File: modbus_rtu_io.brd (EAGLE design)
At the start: 108 x 67.9 mm, 60 parts, among them IC1 MAX3485ESA, IC5 ATMEGA48/88/168-PU, K1 AQY27SMD, K2 AQY22SOP, K3 G6D-1A-ASI12VDC, K4 RP418005, K5 AQG12105, K7 G6D-1A-ASI12VDC, K8 AQY22SOP, T1 BC846, T2 BC846, T4 BC846

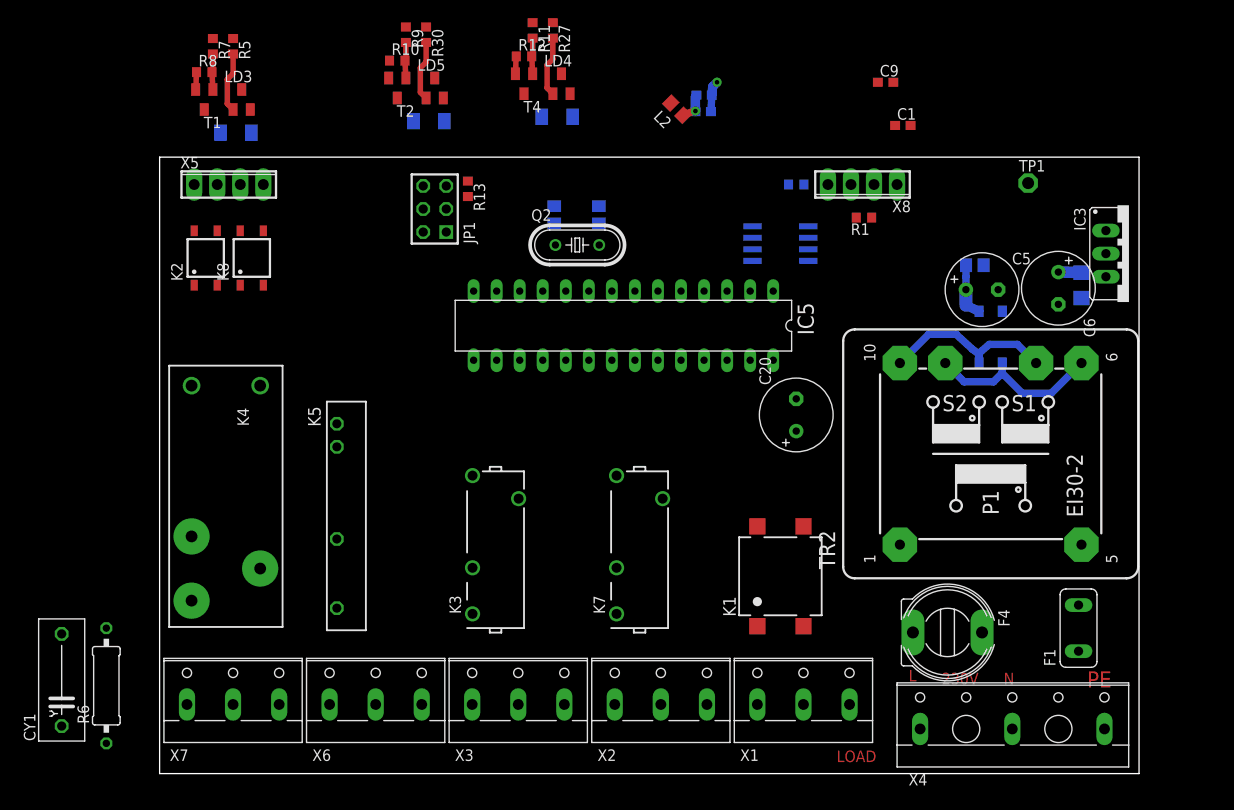
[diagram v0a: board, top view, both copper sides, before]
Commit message: Relais geändert, Routing angefangen
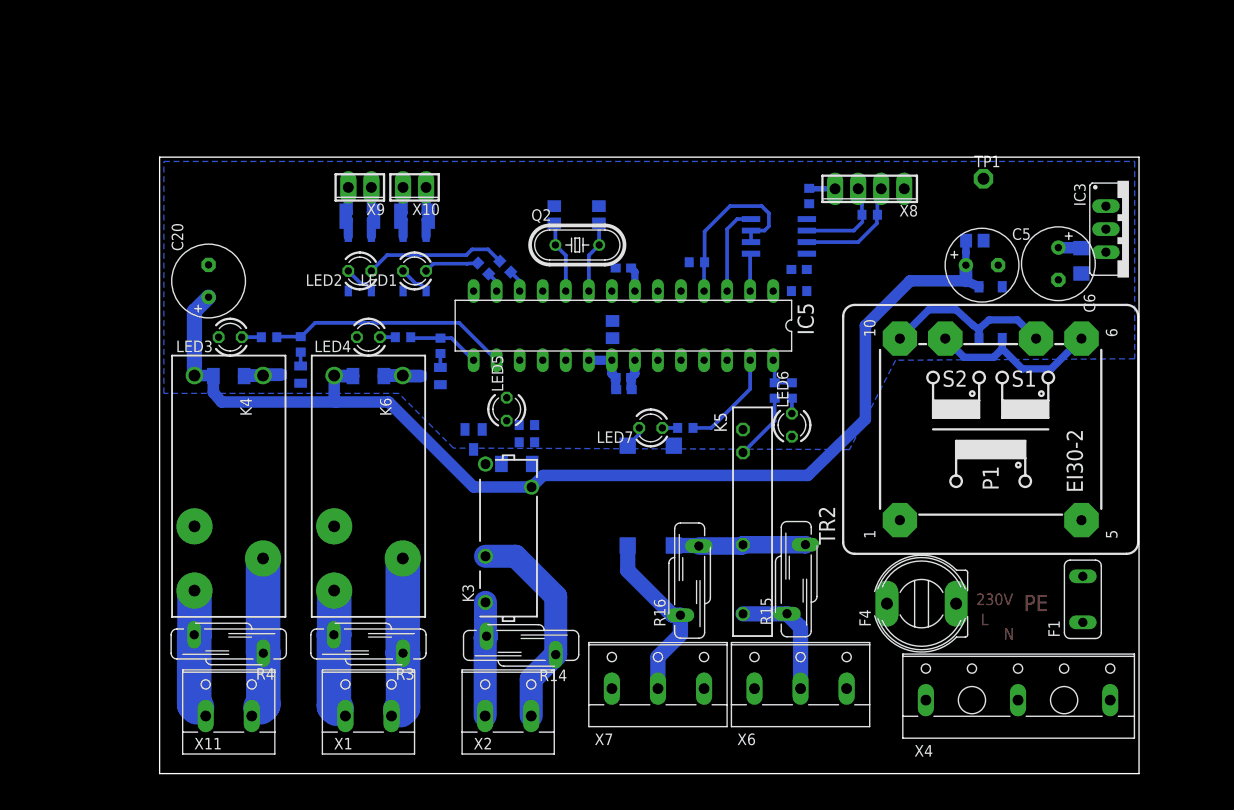
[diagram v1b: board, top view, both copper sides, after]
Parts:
- removed CY1: (no value), rcl:YC10B5
- removed JP1: AVR-ISP-6, atmel:AVR-ISP-6
- removed K7: G6D-1A-ASI12VDC, relay:G6D
- removed LD3, LD4, LD5: PL006-WCR12, led:SOT23
- removed R12: 100K, rcl:R0603
- removed X3: (no value), con-wago-508:W237-133
- removed X5: (no value), con-phoenix-254:4POL254
- added K6: RP418005, relay:RT-C/O12A3.5
- added LED1, LED2, LED3, LED4, LED5, LED6, LED7: (no value), led:LED3MM
- added R14, R15, R16, R3, R4: S10K40, varistor:S10K40
- added R17, R18: VARISTORCN1210, varistor:CT/CN1210
- added R19, R20, R21: 120, rcl:R0603
- added X10, X9: (no value), con-phoenix-254:2POL254
- added X11: (no value), con-wago-508:W237-132
- R10: value 100K -> 120
- R6: value (none) -> 120; device rcl:0309/12 -> rcl:R0603
- R8: value 100K -> 47K
- X1, X2: device con-wago-508:W237-133 -> con-wago-508:W237-132
- moved R6 80.5 mm to (67.8, 42.2), flipped to the bottom, turned to 270 degrees
- moved C20 66.4 mm to (5.40, 54.3)
- moved R8 58.2 mm to (59.2, 56.4), flipped to the bottom
- moved R10 56.7 mm to (69.7, 42.2), flipped to the bottom, turned to 270 degrees
- moved X1 48.0 mm to (23.0, 6.99)
- moved X7 46.9 mm to (54.9, 10.0)
- moved X6 46.9 mm to (70.6, 10.0)
- moved R9 46.9 mm to (40.5, 36.5), flipped to the bottom, turned to 0 degrees
- moved K5 44.8 mm to (64.3, 27.8)
- moved R30 44.4 mm to (40.5, 38.4), flipped to the bottom, turned to 0 degrees
- moved T2 39.6 mm to (34.6, 36.8), flipped to the bottom
- moved D3 39.0 mm to (39.4, 34.1)
- moved R13 38.2 mm to (70.5, 53.2), flipped to the bottom, turned to 180 degrees
- moved R27 37.6 mm to (26.8, 48.1), flipped to the bottom, turned to 0 degrees
- moved R11 36.2 mm to (31.0, 47.1), flipped to the bottom
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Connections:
- removed net DATA: IC5.18, JP1.1
- removed net MOSI: IC5.17, JP1.4
- removed net SCK: IC5.19, JP1.3
- new net AQG12105: IC5.28, R10.1, R6.1
- new net AQY27SMD: IC5.27, R19.1
- new net N$24: K6.11, R3.1, X1.2
- new net N$25: K3.7, R14.2, X2.1
- new net N$26: K3.5, R14.1, X2.2
- new net N$27: K5.O2, R15.1, X6.2
- new net N$29: K1.4, R16.1, X7.2
- new net N$30: K5.+, R6.2
- new net N$31: K1.1, LED7.K
- new net N$32: K2.1, LED2.K
- new net N$35: K8.1, LED1.K
- new net N$37: IC5.12, R20.2
- new net N$38: IC5.13, R21.2
- new net N$4: K4.11, R4.1, X11.2
- new net N$41: LED1.A, R21.1
- new net N$42: LED2.A, R20.1
- new net N$43: LED7.A, R19.2
- new net N$44: LED6.K, R10.2
- new net N$5: K4.14, R4.2, X11.1
- new net N$6: K6.14, R3.2, X1.1
- net +12V: now also K6.A1; no longer K7.13
- net +5V: no longer JP1.2
- net GND: now also K1.2, K2.2, K5.-, K8.2, LED3.K, LED4.K, LED5.K, LED6.A, R8.2; no longer CY1.2, JP1.6, LD3.3, LD4.3, LD5.3, R10.1, R12.1, R6.2, R8.1
- net N$13: no longer R12.2
- net N$14: now also K6.A2; no longer K7.1
- net N$15: now also IC5.4, R8.1
- net N$16: now also R18.1, X10.1; no longer X5.3
- net N$18: now also R18.2, X10.2; no longer X5.4
- net N$2: no longer R10.2
- net N$20: now also R17.1, X9.1; no longer X5.1
- net N$21: now also R17.2, X9.2; no longer X5.2
- net N$28: now also X6.3, X7.3
- net N$3: now also LED3.A; no longer LD3.1
- net N$33: now also K1.3, K5.O1, R15.2, R16.2
- net N$34: now also LED4.A; no longer LD4.1
- net N$36: now also IC5.16
- net N$39: now also IC5.15
- net N$40: now also IC5.17
- net N$50: now also LED5.A; no longer LD5.1
- net N$55: no longer JP1.5
- net N$7: no longer R8.2
- net PE: now also X6.1, X7.1; no longer CY1.1, R6.1
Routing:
- net +12V: track 6.02 -> 127.2 mm
- net N$36: track 0.00 -> 26.6 mm
- net N$26: track 0.00 -> 23.9 mm
- net N$15: track 0.00 -> 20.0 mm
- net N$29: track 0.00 -> 19.7 mm
- net N$24: track 0.00 -> 16.9 mm
- net N$4: track 0.00 -> 16.6 mm
- net N$42: track 0.00 -> 15.7 mm
- net N$33: track 0.00 -> 14.6 mm
- net N$27: track 0.00 -> 13.7 mm
- net N$6: track 0.00 -> 13.2 mm
- net N$5: track 0.00 -> 13.0 mm
- net N$25: track 0.00 -> 12.6 mm
- net RS485_B: track 0.00 -> 12.6 mm
- net AQY27SMD: track 0.00 -> 11.2 mm
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- added copper zone on layer 16, net GND
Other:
- board text removed: "LOAD"

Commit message: routing fertig
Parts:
- removed X4: (no value), con-wago-508:W237-3N
- added C3, C7, C8: 100nF, rcl:C0603
- added LED8: (no value), led:LED3MM
- added R12, R23, R24: 120, rcl:R0603
- added R22: 10K, rcl:R0603
- added SL1: (no value), con-amp-quick:03P
- added SL2: (no value), con-amp-quick:02P
- added X3: GMSTBV3, con-phoenix-762:GMSTBV3
- moved TP1 14.4 mm to (105.3, 65.2)
- moved IC3 14.4 mm to (93.2, 64.5), turned to 0 degrees
- moved F1 12.9 mm to (88.9, 19.4)
- moved X9 9.00 mm to (13.2, 63.2)
- moved R17 8.90 mm to (13.2, 61.1)
- moved K2 8.89 mm to (13.2, 56.2)
- moved LED2 8.89 mm to (13.2, 55.4)
- moved X10 8.07 mm to (20.2, 63.2)
- moved R18 7.94 mm to (20.2, 61.1)
- moved K8 7.94 mm to (20.2, 56.2)
- moved LED1 7.94 mm to (20.2, 55.4)
- moved R9 7.31 mm to (34.4, 40.6)
- moved F4 4.00 mm to (80.0, 18.3)
- moved R30 3.62 mm to (37.6, 40.6), turned to 180 degrees
- moved R1 2.93 mm to (76.0, 59.7)
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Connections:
- new net N$45: R12.1, X8.1
- new net N$51: LED8.K, R22.2
- new net N$53: C7.1, IC5.6, R23.1, SL1.1
- new net N$56: C8.2, IC5.23, R24.2, SL2.2
- net +12V: now also R12.2
- net +5V: now also C3.1, LED8.A, R23.2, SL1.3, SL2.1
- net GND: now also C3.2, C7.2, C8.1, R22.1, R24.1, SL1.2
- net L: now also X3.2; no longer X4.1
- net N$23: now also TR2.1; no longer TR2.5
- net N$28: now also TR2.5, X3.3; no longer TR2.1, X4.2
- net PE: now also X3.1; no longer X4.3
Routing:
- net N$28: track 0.00 -> 76.6 mm
- net PE: track 0.00 -> 51.0 mm
- net N$56: track 0.00 -> 37.9 mm
- net +5V: track 5.26 -> 41.3 mm, vias 0 -> 1
- net N$26: track 23.9 -> 45.7 mm
- net L: track 0.00 -> 18.1 mm
- net N$49: track 0.00 -> 15.7 mm
- net N$47: track 0.00 -> 15.6 mm
- net +12V: track 127.2 -> 142.4 mm
- net N$48: track 0.00 -> 12.3 mm
- net N$46: track 0.00 -> 11.9 mm
- net N$23: track 0.00 -> 11.0 mm
- net N$25: track 12.6 -> 23.0 mm
- net N$53: track 0.00 -> 8.97 mm
- net N$42: track 15.7 -> 24.6 mm
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- added copper zone on layer 1, net +5V
- added copper zone on layer 1, net GND

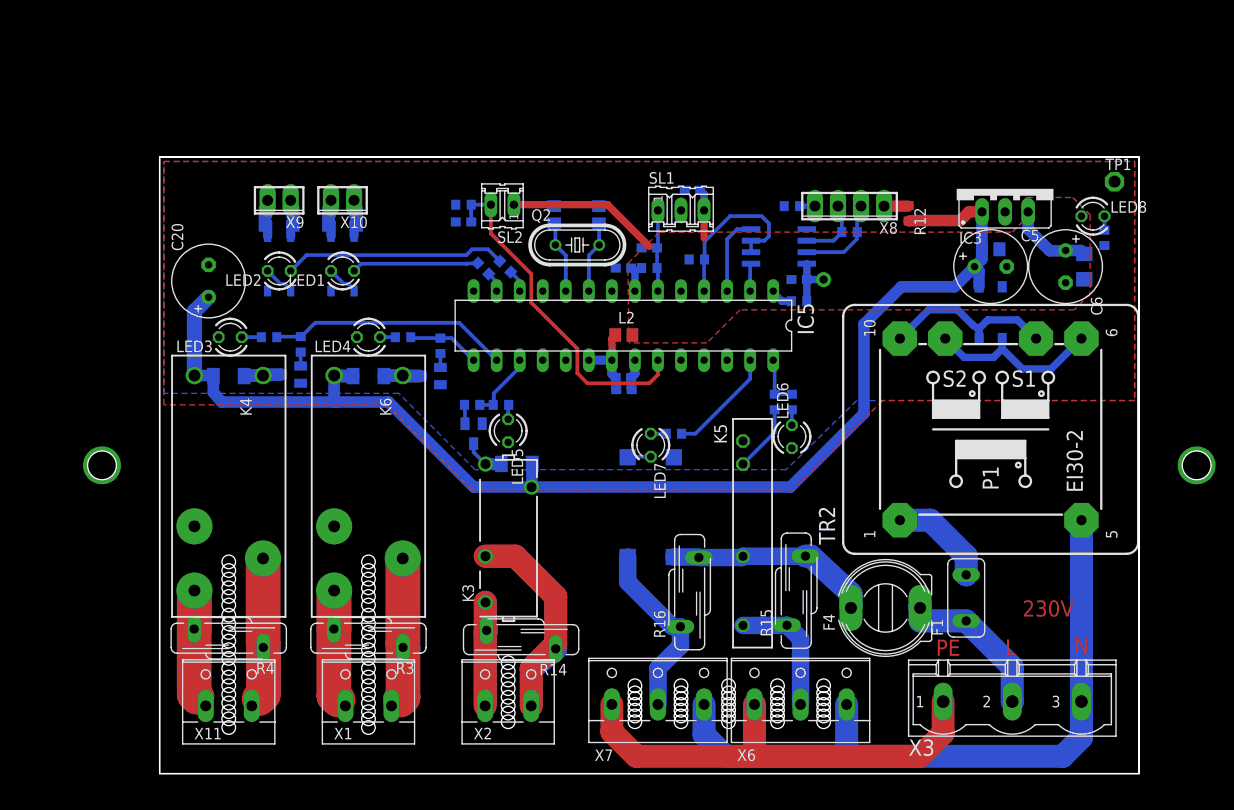
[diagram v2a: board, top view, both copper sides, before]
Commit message: opto-mosfet package berichtigt, fertigung vorbereitet
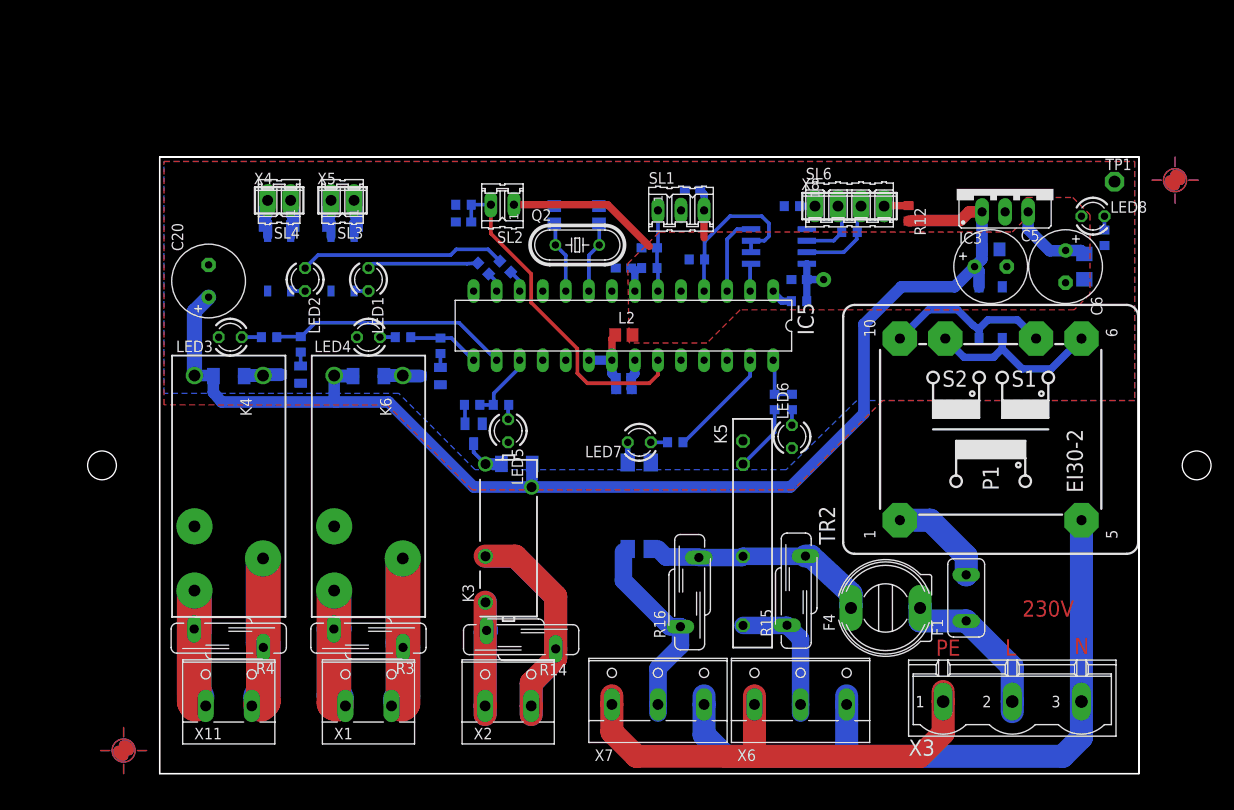
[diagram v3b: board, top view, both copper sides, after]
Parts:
- removed K1: AQY27SMD, relay:AQY27-SMD04
- added OK8: (no value), optocoupler:DIL4-SMD
- added SL3, SL4: (no value), con-amp-quick:02P
- added SL6: (no value), con-amp-quick:04P
- added U$1, U$2: (no value), marks:PASS-ROUND
- moved LED1 3.01 mm to (23.0, 54.5), turned to 270 degrees
- moved LED2 3.01 mm to (16.0, 54.5), turned to 270 degrees
- moved LED7 1.31 mm to (52.9, 36.5), turned to 180 degrees
- moved R19 0.97 mm to (56.8, 36.5)
- turned X4 to 0 degrees
- turned X5 to 0 degrees
- turned X8 to 0 degrees
- renumbered X10 to X5, X9 to X4
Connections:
- net GND: now also OK8.2; no longer K1.2
- net N$16: now also SL3.1; no longer X5.1
- net N$18: now also SL3.2; no longer X5.2
- net N$20: now also SL4.1; no longer X4.1
- net N$21: now also SL4.2; no longer X4.2
- net N$29: now also OK8.4; no longer K1.4
- net N$31: now also OK8.1; no longer K1.1
- net N$33: now also OK8.3; no longer K1.3
- net N$45: now also SL6.4; no longer X8.1
- net N$8: now also SL6.1; no longer X8.4
- net RS485_A: now also SL6.2; no longer X8.3
- net RS485_B: now also SL6.3; no longer X8.2
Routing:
- net PE: track 51.0 -> 54.0 mm
- net N$33: track 22.8 -> 25.7 mm
- net N$29: track 20.2 -> 22.7 mm
- net N$32: track 3.54 -> 1.59 mm
- net N$35: track 3.54 -> 1.59 mm
- net N$28: track 76.6 -> 78.5 mm
- net N$25: track 23.0 -> 24.9 mm
- net N$26: track 45.7 -> 47.4 mm
- net N$41: track 14.0 -> 12.3 mm
- net N$42: track 24.6 -> 22.9 mm
- net N$24: track 15.7 -> 17.3 mm
- net N$4: track 15.4 -> 16.8 mm
- net N$5: track 11.9 -> 13.3 mm
- net N$6: track 12.1 -> 13.3 mm
- net L: track 18.1 -> 19.2 mm
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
